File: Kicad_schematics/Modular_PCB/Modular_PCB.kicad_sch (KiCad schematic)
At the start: 4 parts

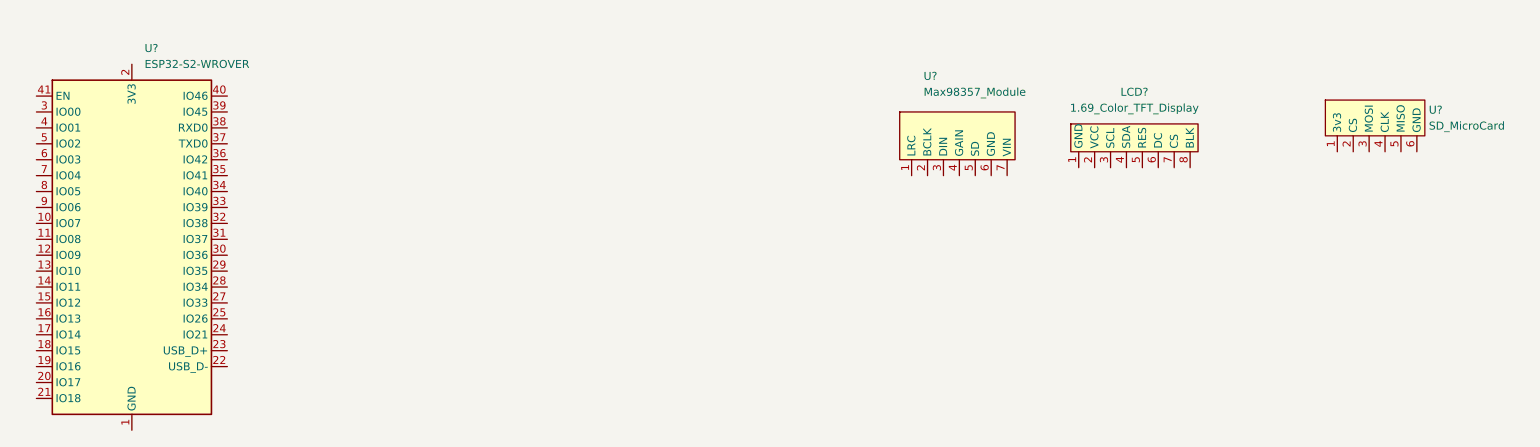
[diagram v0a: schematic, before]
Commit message: Add: KiCad base project with all footprints and symbols
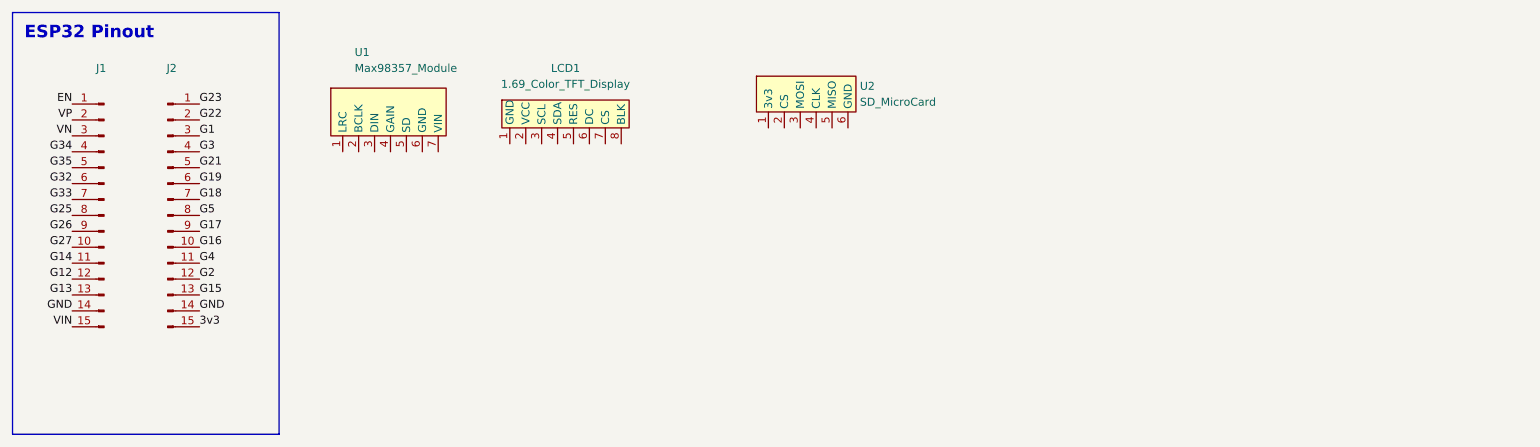
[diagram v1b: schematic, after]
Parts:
- removed U?: ESP32-S2-WROVER, RF_Module:ESP32-S2-WROVER, symbol RF_Module:ESP32-S2-WROVER
- added J1, J2: Conn_01x15_Male, Connector_PinSocket_2.54mm:PinSocket_1x15_P2.54mm_Vertical, symbol Connector:Conn_01x15_Male
- LCD1: renamed from LCD?; footprint (none) -> Mini_Tv_ESP32:Display_TFT
- U1: renamed from U?; footprint (none) -> Mini_Tv_ESP32:Max98357_Module
- U2: renamed from U?; footprint (none) -> Mini_Tv_ESP32:MicroSDModule
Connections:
- new net 3v3: J2.15 (Pin_15)
- new net EN: J1.1 (Pin_1)
- new net G1: J2.3 (Pin_3)
- new net G12: J1.12 (Pin_12)
- new net G13: J1.13 (Pin_13)
- new net G14: J1.11 (Pin_11)
- new net G15: J2.13 (Pin_13)
- new net G16: J2.10 (Pin_10)
- new net G17: J2.9 (Pin_9)
- new net G18: J2.7 (Pin_7)
- new net G19: J2.6 (Pin_6)
- new net G2: J2.12 (Pin_12)
- new net G21: J2.5 (Pin_5)
- new net G22: J2.2 (Pin_2)
- new net G23: J2.1 (Pin_1)
- new net G25: J1.8 (Pin_8)
- new net G26: J1.9 (Pin_9)
- new net G27: J1.10 (Pin_10)
- new net G3: J2.4 (Pin_4)
- new net G32: J1.6 (Pin_6)
- new net G33: J1.7 (Pin_7)
- new net G34: J1.4 (Pin_4)
- new net G35: J1.5 (Pin_5)
- new net G4: J2.11 (Pin_11)
- new net G5: J2.8 (Pin_8)
- new net GND: J1.14 (Pin_14), J2.14 (Pin_14)
- new net VIN: J1.15 (Pin_15)
- new net VN: J1.3 (Pin_3)
- new net VP: J1.2 (Pin_2)
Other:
- note added: "ESP32 Pinout"
- moved on the sheet: LCD1, U1, U2
